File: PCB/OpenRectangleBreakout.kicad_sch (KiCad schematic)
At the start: 43 parts, among them J1 USB C Connector, J2 JTAG_TC2030, J3 Conn_01x04_Pin, J4 Conn_01x04_Pin, J5 Conn_01x06_Pin, SW1 Boot, U1 XC6206, U2 USBLC6-2SC6, U3 RP2040, U4 W25Q128JVS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

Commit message: First version
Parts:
- added H1: MountingHole_Pad, MountingHole:MountingHole_2.2mm_M2_ISO14580_Pad, symbol Mechanical:MountingHole_Pad
- added H2, H3, H4, H5, H6: MountingHole, MountingHole:MountingHole_2.1mm, symbol Mechanical:MountingHole
- added J6, J7, J8: Screw_Terminal_01x09, Connector_PinHeader_2.54mm:PinHeader_1x09_P2.54mm_Vertical, symbol Connector:Screw_Terminal_01x09
- D3: LCSC (none) -> C2297
- J5: value Conn_01x06_Pin -> GCC Cable; footprint Connector_PinHeader_2.54mm:PinHeader_1x06_P2.54mm_Vertical -> Connector_PinHeader_2.00mm:PinHeader_1x06_P2.00mm_Vertical
- R4: LCSC (none) -> C25117
- R5, R6: footprint Resistor_SMD:R_0603_1608Metric -> Resistor_SMD:R_0402_1005Metric
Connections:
- net A: now also J7.4 (Pin_4)
- net B: now also J8.3 (Pin_3)
- net C_DN: now also J7.2 (Pin_2)
- net C_LT: now also J7.3 (Pin_3)
- net C_RT: now also J7.6 (Pin_6)
- net C_UP: now also J7.5 (Pin_5)
- net DOWN: now also J6.4 (Pin_4)
- net GND: now also J6.1 (Pin_1), J7.1 (Pin_1), J8.1 (Pin_1)
- net L: now also J6.2 (Pin_2)
- net LEFT: now also J6.3 (Pin_3)
- net LS: now also J8.6 (Pin_6)
- net M1: now also J6.6 (Pin_6)
- net M2: now also J6.7 (Pin_7)
- net MS: now also J8.8 (Pin_8)
- net R: now also J8.2 (Pin_2)
- net RIGHT: now also J6.5 (Pin_5)
- net START: now also J6.8 (Pin_8)
- net UP: now also J8.9 (Pin_9)
- net X: now also J8.5 (Pin_5)
- net Y: now also J8.4 (Pin_4)
- net Z: now also J8.7 (Pin_7)
- net 8: now reaches U3.11 (GPIO8)
- net 8: now also J6.9 (Pin_9)
- net 9: now reaches U3.12 (GPIO9)
- net 9: now also J7.7 (Pin_7)
- net SELECT: now reaches U3.13 (GPIO10)
- net SELECT: now also J7.8 (Pin_8)
- net HOME: now reaches U3.14 (GPIO11)
- net HOME: now also J7.9 (Pin_9)
- net Earth: now reaches J1.S1 (SHIELD), R1.2
- net Earth: now also H1.1
- no-connect marks 13 -> 9
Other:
- note added: "Mounting"
- note added: "Open Rectangle Breakout by Quark Use responsibly!"
- note removed: "Open Rectangle Template by Quark Use responsibly!"
- moved on the sheet: R1

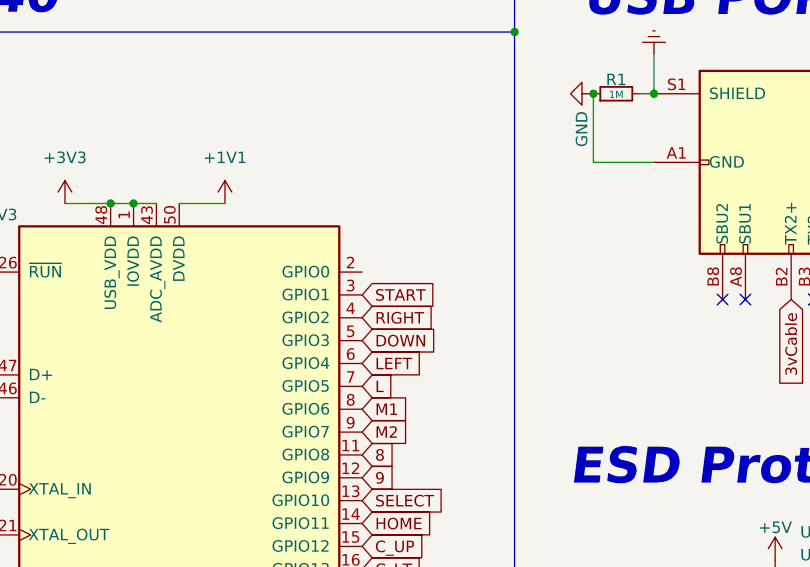
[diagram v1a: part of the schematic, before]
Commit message: Fixed START button to the correct pin
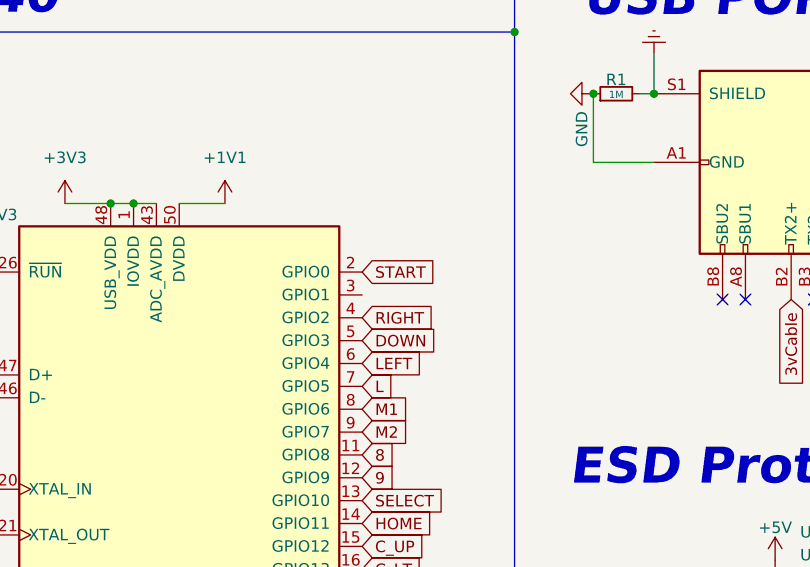
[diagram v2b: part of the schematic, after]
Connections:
- net START: now also U3.2 (GPIO0); no longer U3.3 (GPIO1)
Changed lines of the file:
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@@
     )
   )
-  (global_label "START" (shape input) (at 71.7108 51.308 0) (fields_autoplaced)
+  (global_label "START" (shape input) (at 71.7108 48.768 0) (fields_autoplaced)
     (effects (font (size 1.27 1.27)) (justify left))
-    (property "Intersheetrefs" "${INTERSHEET_REFS}" (at 79.6272 51.2286 0)
+    (property "Intersheetrefs" "${INTERSHEET_REFS}" (at 79.6272 48.6886 0)
       (effects (font (size 1.27 1.27)) (justify left) hide)
     )
